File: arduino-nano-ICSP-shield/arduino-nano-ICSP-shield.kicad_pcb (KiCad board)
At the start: 2 copper layers, 43.2 x 17.8 mm, 6 parts, among them J1 Analog, J2 Digital

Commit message: init led's
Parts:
- added D1: LED, LED_SMD:LED_0805_2012Metric_Pad1.15x1.40mm_HandSolder, F.Cu at (104.0, 88.0)
- added D2: LED, LED_SMD:LED_0805_2012Metric_Pad1.15x1.40mm_HandSolder, F.Cu at (104.0, 91.5)
- added D3: LED, LED_SMD:LED_0805_2012Metric_Pad1.15x1.40mm_HandSolder, F.Cu at (104.0, 95.0)
- added R1: R, Resistor_SMD:R_0805_2012Metric_Pad1.20x1.40mm_HandSolder, B.Cu at (110.2, 88.0)
- added R2: R, Resistor_SMD:R_0805_2012Metric_Pad1.20x1.40mm_HandSolder, B.Cu at (110.2, 91.5)
- added R3: R, Resistor_SMD:R_0805_2012Metric_Pad1.20x1.40mm_HandSolder, B.Cu at (110.2, 95.0)
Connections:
- J2 pad 4: /*D9 -> heartbeat
- J2 pad 5: /D8 -> error
- J2 pad 6: /D7 -> programming
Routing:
- net GND: track 0.00 -> 49.0 mm, vias 0 -> 2
- net programming: track 0.00 -> 23.8 mm, vias 0 -> 1
- net /~{RESET}: track 0.00 -> 15.2 mm
- net error: track 0.00 -> 12.5 mm
- net Net-(D2-K): track 0.00 -> 8.94 mm, vias 0 -> 1
- net Net-(D3-K): track 0.00 -> 8.93 mm, vias 0 -> 1
- net Net-(D1-K): track 0.00 -> 8.88 mm, vias 0 -> 1
- net heartbeat: track 0.00 -> 8.48 mm
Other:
- board text added: "Error"
- board text added: "Heartbeat"
- board text added: "Programming"

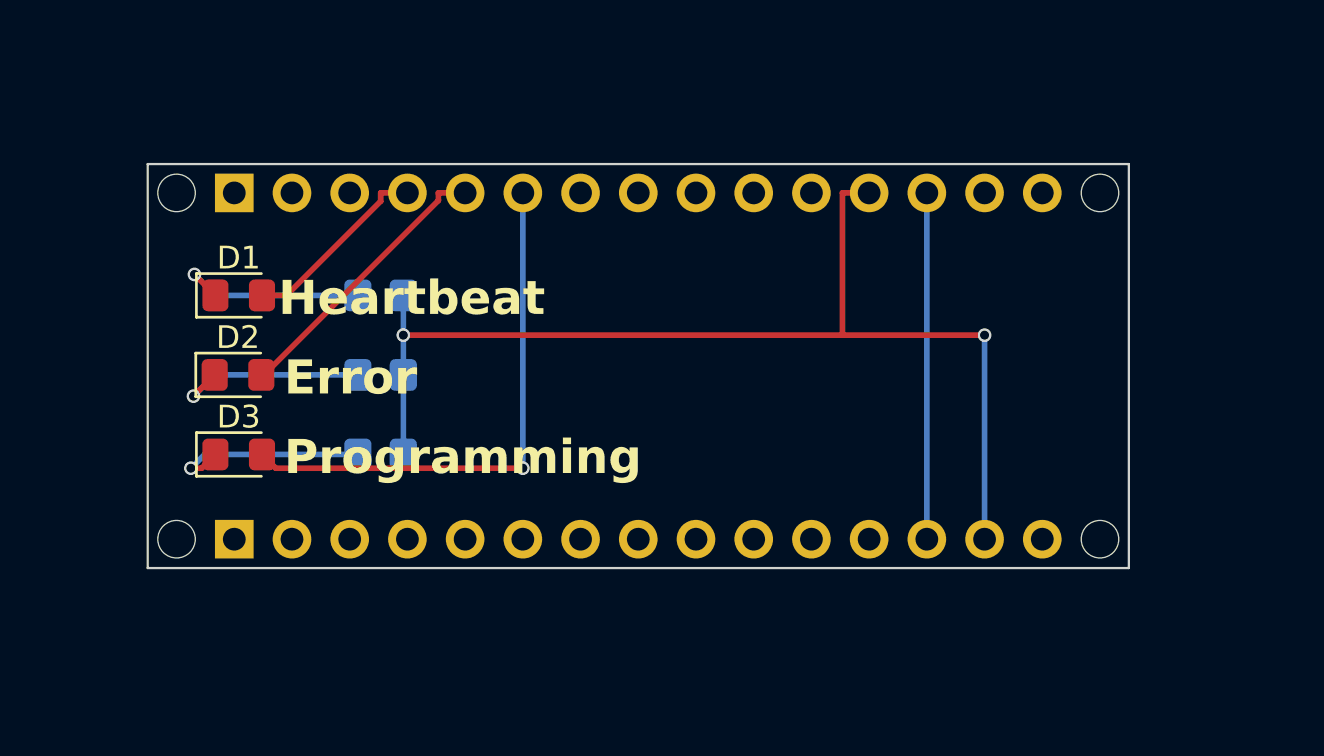
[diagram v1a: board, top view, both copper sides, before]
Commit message: add ports
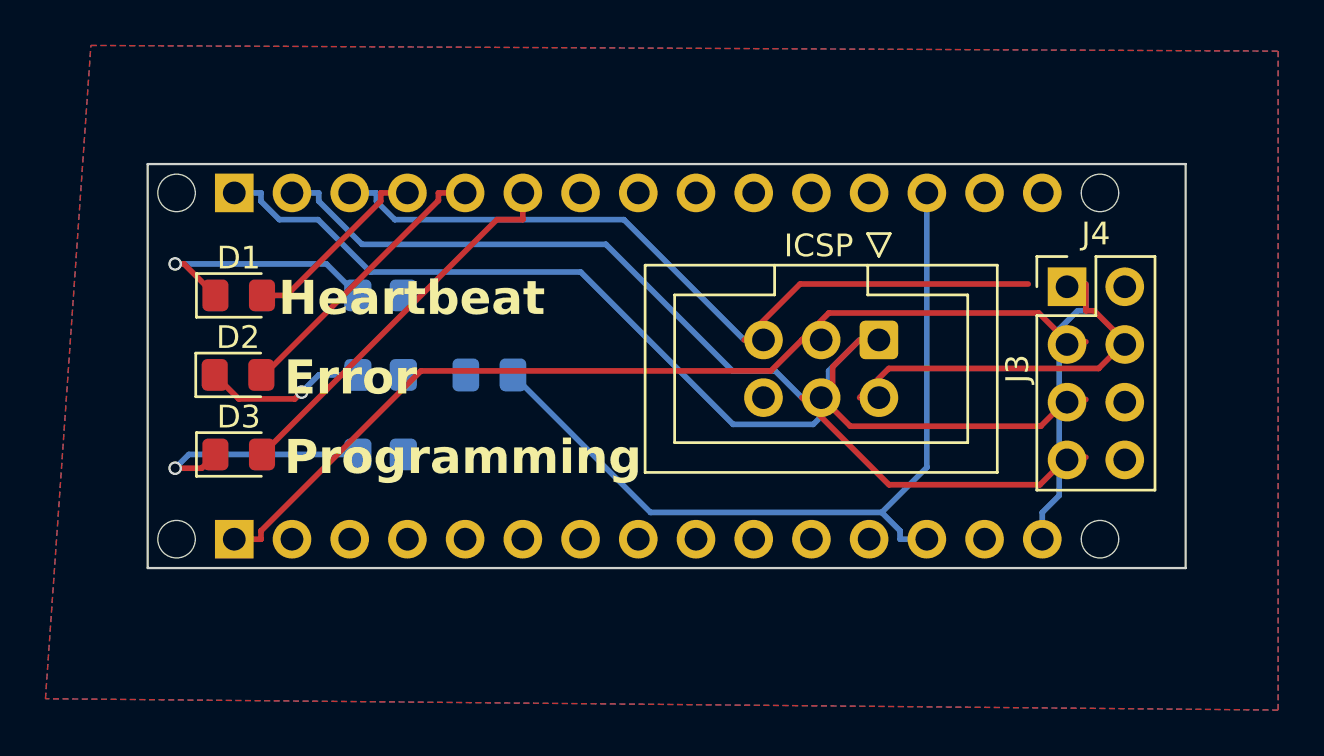
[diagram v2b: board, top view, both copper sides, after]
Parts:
- added C1: 10µF, Capacitor_SMD:C_0805_2012Metric_Pad1.18x1.45mm_HandSolder, B.Cu at (115.0, 91.5)
- added J3: AVR-ISP-6, Connector_IDC:IDC-Header_2x03_P2.54mm_Vertical, F.Cu at (132.2, 90.0)
- added J4: Conn_02x04_Counter_Clockwise, CustomLibrary:PinHeader_2x04_P2.54mm_Vertical_Counterclockwise, F.Cu at (140.5, 87.6)
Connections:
- J1 pad 1: /D13/SCK -> sck
- J2 pad 1: /D12/MISO -> miso
- J2 pad 2: /*D11/MOSI -> mosi
- J2 pad 3: /*D10/SS -> reset
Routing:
- net miso: track 0.00 -> 50.2 mm
- net GND: track 49.0 -> 0.00 mm, vias 2 -> 0
- net sck: track 0.00 -> 42.6 mm
- net mosi: track 0.00 -> 41.2 mm
- net reset: track 0.00 -> 33.8 mm
- net VCC: track 0.00 -> 28.0 mm
- net /~{RESET}: track 15.2 -> 36.3 mm
- net programming: track 23.8 -> 16.9 mm, vias 1 -> 0
- net Net-(D1-K): track 8.88 -> 11.0 mm
- net Net-(D2-K): track 8.94 -> 7.18 mm
- net Net-(D3-K): track 8.93 -> 10.3 mm
- added copper zone on B.Cu, net GND
- added copper zone on F.Cu, net GND
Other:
- board size 43.2 x 17.8 mm -> 45.7 x 17.8 mm

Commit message: single header
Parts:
- removed J4: Conn_02x04_Counter_Clockwise, CustomLibrary:PinHeader_2x04_P2.54mm_Vertical_Counterclockwise
- J3: footprint Connector_IDC:IDC-Header_2x03_P2.54mm_Vertical -> CustomLibrary:IDC-Header_2x03_P2.54mm_Vertical-ICSP-6
- moved J3 0.93 mm to (133.1, 90.2)
- moved D1 0.66 mm to (103.3, 88.0)
- moved D2 0.66 mm to (103.3, 91.5)
- moved D3 0.66 mm to (103.3, 95.0)
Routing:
- net reset: track 33.8 -> 15.9 mm
- net mosi: track 41.2 -> 35.4 mm
- net sck: track 42.6 -> 47.3 mm
- net VCC: track 28.0 -> 24.7 mm
- net miso: track 50.2 -> 48.6 mm
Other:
- board size 45.7 x 17.8 mm -> 43.2 x 17.8 mm
